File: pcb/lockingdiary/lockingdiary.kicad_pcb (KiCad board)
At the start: 2 copper layers, 9 parts, among them J1 Power_Socket, J2 Keypad_Socket, J3 Servo_Socket, J4 Every_Nano_LeftHdr, J5 Every_Nano_RightHdr

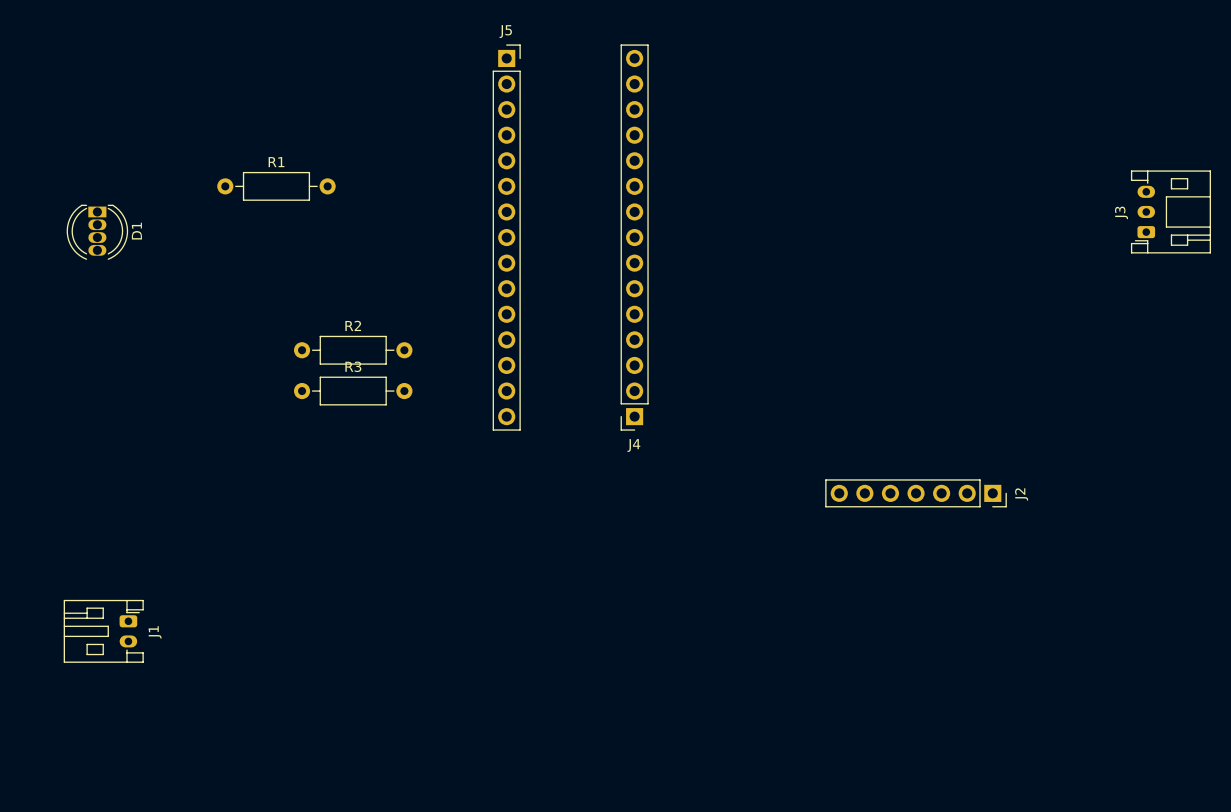
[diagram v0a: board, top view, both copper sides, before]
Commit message: Finished rev1 PCB design. Started on readme and docs
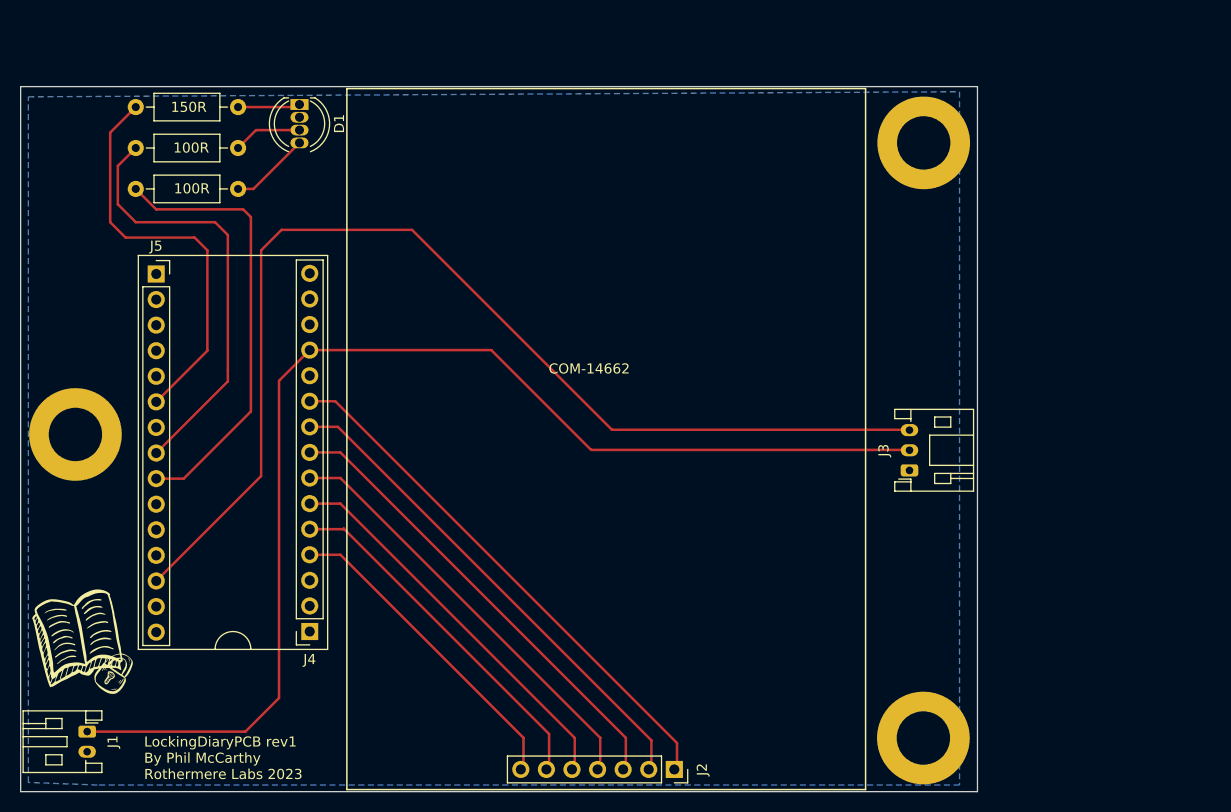
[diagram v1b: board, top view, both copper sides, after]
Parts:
- added G***: LOGO, logo:lockingdiarylogo, F.Cu at (112.8, 121.4)
- added REF**: MountingHole_5.3mm_M5_DIN965_Pad, MountingHole:MountingHole_5.3mm_M5_DIN965_Pad, F.Cu at (196.3, 131.0)
- added REF**: MountingHole_5.3mm_M5_DIN965_Pad, MountingHole:MountingHole_5.3mm_M5_DIN965_Pad, F.Cu at (196.3, 71.9)
- added REF**: MountingHole_5.3mm_M5_DIN965_Pad, MountingHole:MountingHole_5.3mm_M5_DIN965_Pad, F.Cu at (112.1, 100.8)
- moved J2 41.8 mm to (171.6, 134.1)
- moved J5 40.8 mm to (120.1, 84.9)
- moved J4 38.7 mm to (135.4, 120.4)
- moved J3 33.4 mm to (194.9, 104.4)
- moved D1 22.7 mm to (134.4, 68.1)
- moved R2 21.1 mm to (128.3, 72.4), turned to 180 degrees
- moved R3 21.0 mm to (128.3, 76.5), turned to 180 degrees
- moved J1 11.7 mm to (113.3, 130.3)
- moved R1 7.98 mm to (128.3, 68.3), turned to 180 degrees
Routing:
- net +5V: track 0.00 -> 119.6 mm
- net /ServoPWM: track 0.00 -> 110.3 mm
- net /keys_c2: track 0.00 -> 53.1 mm
- net /keys_r1: track 0.00 -> 49.7 mm
- net /keys_c1: track 0.00 -> 46.3 mm
- net /Blue: track 0.00 -> 44.0 mm
- net /Green: track 0.00 -> 43.1 mm
- net /keys_r4: track 0.00 -> 42.7 mm
- net /Red: track 0.00 -> 40.4 mm
- net /keys_c3: track 0.00 -> 39.1 mm
- net /keys_r3: track 0.00 -> 35.8 mm
- net /keys_r2: track 0.00 -> 31.9 mm
- net Net-(D1-BA): track 0.00 -> 7.99 mm
- net Net-(D1-GA): track 0.00 -> 6.83 mm
- net Net-(D1-RA): track 0.00 -> 6.20 mm
- added copper zone on B.Cu, net GND
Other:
- board outline added: 95 x 70 mm
- board text added: "COM-14662"
- board text added: "LockingDiaryPCB rev1 By Phil McCarthy Rothermere Labs 2023"
